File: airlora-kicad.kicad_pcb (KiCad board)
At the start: 4 copper layers, 77 x 77 mm, 128 parts, among them IC1 BALFHB-WL-02D3, J1 12V, J10 I2C, J11 UART2, J2 Conn_Coaxial, J3 Led, J4 SHT, J5 I2C, J6 A_NO2, J7 UART1, J8 A_CO, J9 I2C, Q1 ZVP2106GTA, Q10 S8050, Q2 S8050, Q3 S8050, Q4 S8050, Q5 S8050, Q6 S8050, Q7 S8050, Q8 S8050, Q9 S8050, SW1 SW_Push, SW2 SW_Slide_DPDT, SW3 SW_Push, U1 TPS7A2633DRVR, U2 TPS54202DDC, U3 TPS7A2633DRVR, U4 BGS12WN6E6327, U5 STM32WLE5CCUx, U6 STM32F103C8Tx, X1 NX2016SA-32MHZ, Y1 NX2012SA 32.768KHz, Y2 8Mhz

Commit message: refactored project
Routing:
- net +5V: track 134.0 -> 0.00 mm
- net /AirLora V3/MCU Sub/SDA1: track 80.1 -> 0.00 mm
- net +3.3V_HP: track 70.0 -> 0.00 mm
- net /AirLora V3/MCU Sub/SCL1: track 64.9 -> 0.00 mm
- net /AirLora V3/MCU Sub/RX3: track 41.3 -> 0.00 mm
- net /AirLora V3/MCU Sub/TX3: track 41.2 -> 0.00 mm
- net /AirLora V3/MCU Sub/PA5: track 30.9 -> 0.00 mm
- net /AirLora V3/MCU Sub/PA15: track 21.1 -> 0.00 mm
- net /AirLora V3/MCU Sub/SW_CLK: track 19.4 -> 0.00 mm
- net Net-(U6-NRST): track 16.4 -> 0.00 mm
- net Net-(D1-A): track 15.2 -> 0.00 mm
- net /AirLora V3/MCU Sub/PB4: track 14.9 -> 0.00 mm
- net Net-(J4-Pin_2): track 14.3 -> 0.00 mm
- net +3.3V: track 13.8 -> 0.00 mm
- net Net-(U2-FB): track 13.7 -> 0.00 mm
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- removed copper zone on B.Cu, net GND
- removed copper zone on F.Cu, net GND
- removed copper zone on In1.Cu, net GND
- removed copper zone on In2.Cu, net GND

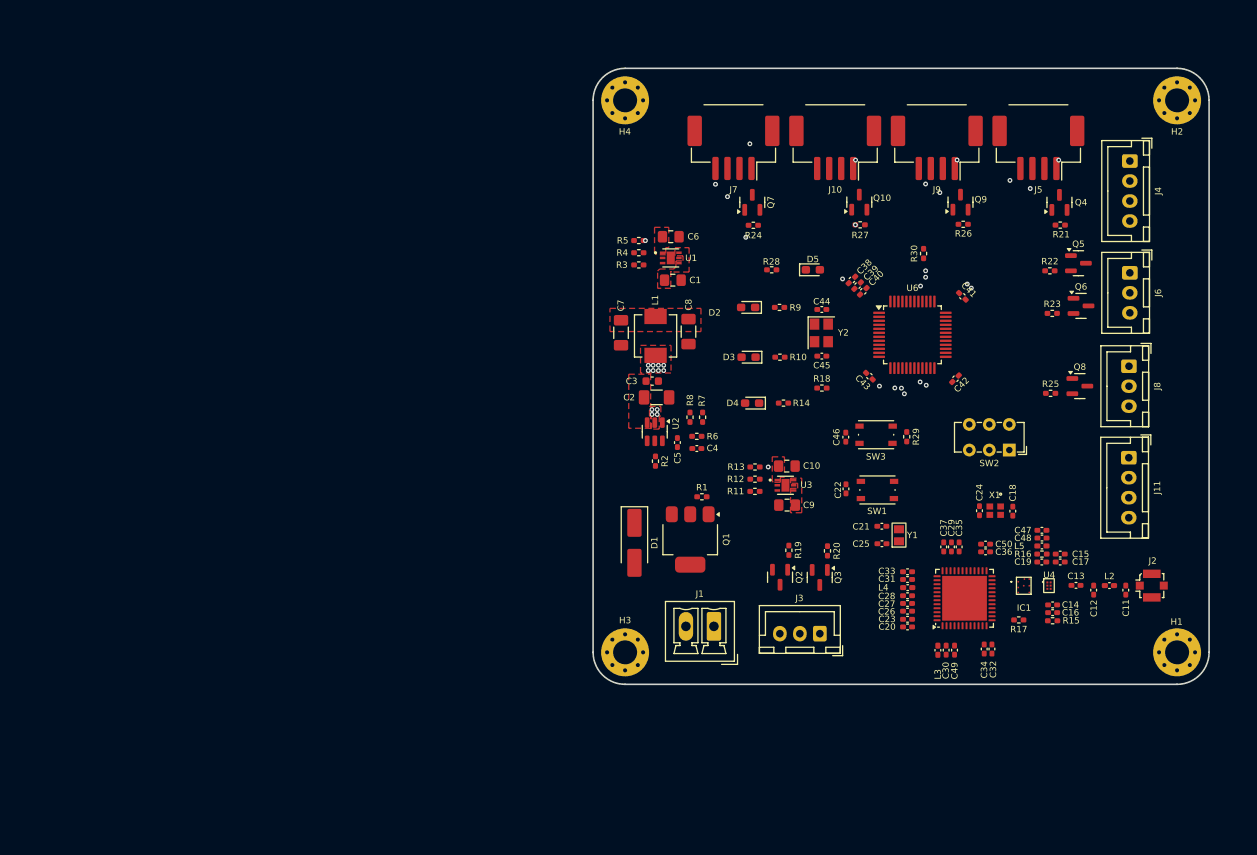
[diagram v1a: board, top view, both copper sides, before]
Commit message: removed polarity protection and fixed component placement
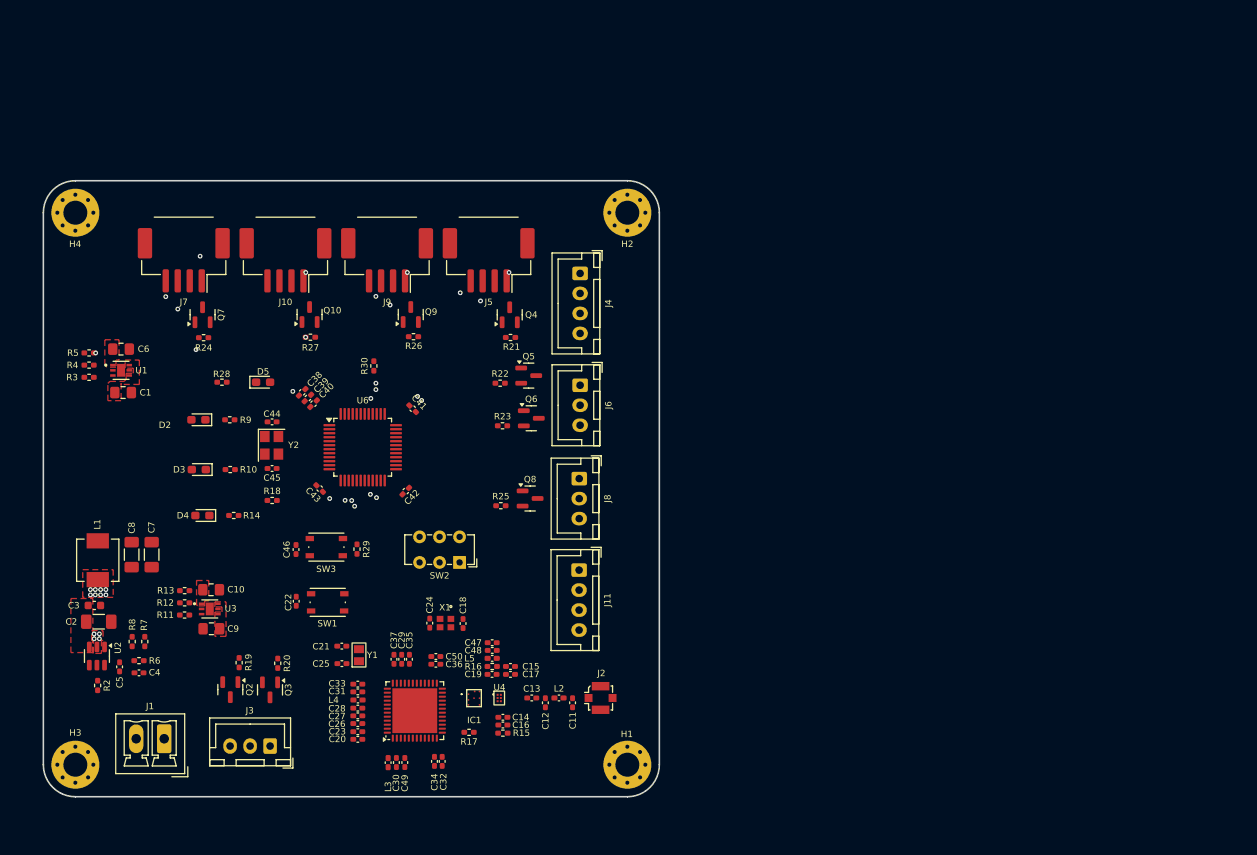
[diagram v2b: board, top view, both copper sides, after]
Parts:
- removed D1: D_Zener, Diode_SMD:D_SMA_Handsoldering
- removed Q1: ZVP2106GTA, Package_TO_SOT_SMD:SOT-223-3_TabPin2
- removed R1: 10K, Resistor_SMD:R_0402_1005Metric_Pad0.72x0.64mm_HandSolder
- C11, C12: value 3.3pF -> NC
- C15, C16: value 10pF -> 100nF
- L2: value 8.7uH -> 0R
- moved C3 75.2 mm to (66.9, 100.9)
- moved L1 75.2 mm to (67.3, 95.2)
- moved R8 75.2 mm to (71.6, 105.4)
- moved C2 75.2 mm to (67.5, 102.9)
- moved C4 75.2 mm to (72.5, 109.3)
- moved C5 75.2 mm to (70.1, 108.6)
- moved R2 75.2 mm to (67.3, 110.9)
- moved R6 75.2 mm to (72.5, 107.8)
- moved R7 75.2 mm to (73.2, 105.4)
- moved U2 75.2 mm to (67.2, 107.2)
- moved C8 75.0 mm to (71.6, 94.5)
- moved C10 73.6 mm to (81.5, 98.9)
- moved C9 73.6 mm to (81.5, 103.8)
- moved U3 73.6 mm to (81.3, 101.3)
- moved R11 72.9 mm to (78.2, 102.1)
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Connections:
- net SW renamed Net-(U2-SW)
- J1 pad 1: Net-(J1-Pin_1) -> +12V
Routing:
- net GND: vias 4 -> 3

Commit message: Update layout PCB
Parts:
- moved C49 1.74 mm to (104.0, 120.5)
- moved C30 1.71 mm to (103.0, 120.5)
- moved L3 1.36 mm to (105.0, 120.5)
- moved C29 0.61 mm to (105.9, 107.6)
- moved C35 0.61 mm to (106.9, 107.6)
- moved C37 0.61 mm to (105.0, 107.6)
- moved R14 0.50 mm to (83.8, 89.6)
- moved D4 0.50 mm to (79.9, 89.6)
- moved C1 0.17 mm to (70.5, 74.1), turned to 180 degrees
- moved D3 0.05 mm to (79.9, 83.9)
- moved R10 0.05 mm to (83.8, 83.9)
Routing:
- net +5V: track 0.00 -> 174.9 mm, vias 4 -> 8
- net +3.3V: track 0.00 -> 128.3 mm, vias 0 -> 5
- net +3.3V_HP: track 0.00 -> 98.8 mm, vias 1 -> 0
- net /AirLora V3/MCU Sub/SCL1: track 0.00 -> 73.8 mm, vias 2 -> 0
- net /AirLora V3/MCU Sub/SDA1: track 0.00 -> 60.0 mm, vias 2 -> 3
- net /AirLora V3/MCU Sub/SCL2: track 0.00 -> 59.1 mm, vias 1 -> 0
- net /AirLora V3/MCU Sub/SDA2: track 0.00 -> 58.4 mm, vias 1 -> 2
- net Net-(U5-PA4): track 0.00 -> 52.8 mm, vias 0 -> 2
- net /AirLora V3/MCU/PA3: track 0.00 -> 52.7 mm, vias 0 -> 2
- net Net-(U5-PA5): track 0.00 -> 47.4 mm
- net /AirLora V3/MCU Sub/TX3: track 0.00 -> 46.5 mm
- net /AirLora V3/MCU Sub/RX3: track 0.00 -> 45.3 mm
- net Net-(U5-PA6): track 0.00 -> 43.4 mm
- net +12V: track 0.00 -> 40.1 mm
- net /AirLora V3/MCU Sub/PB0: track 0.00 -> 36.5 mm, vias 0 -> 1
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- added copper zone on B.Cu, net GND
- added copper zone on F.Cu, net GND
- added copper zone on In1.Cu, net GND
- added copper zone on In2.Cu, net GND

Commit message: Update PCB layout
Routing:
- net +12V: track 40.1 -> 42.0 mm
- net +3.3V: track 128.3 -> 129.1 mm
- net /AirLora V3/MCU Sub/PB0: track 36.5 -> 35.7 mm
- net Net-(J4-Pin_2): track 14.4 -> 15.0 mm
- net /AirLora V3/MCU Sub/PA5: track 34.8 -> 34.2 mm
- net /AirLora V3/MCU Sub/PA7: track 28.2 -> 28.8 mm
- net Net-(J3-Pin_2): track 7.68 -> 7.14 mm
- net GND: vias 36 -> 37

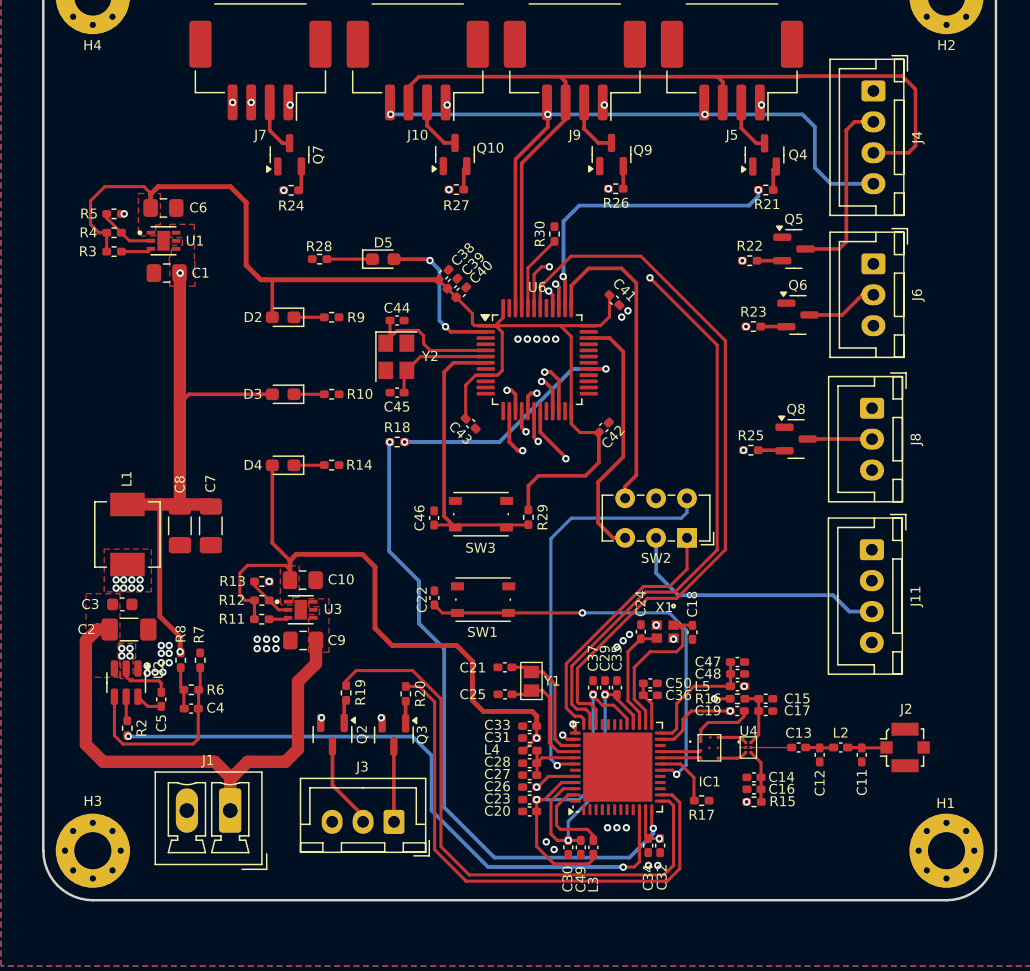
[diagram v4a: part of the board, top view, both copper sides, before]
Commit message: [Fix] Schematic and layout. - Replaced STM32WLE5x symbol for better visualization of the symbols - Added some missing connections - Modified some components' values - Changed the layout for STM32WL
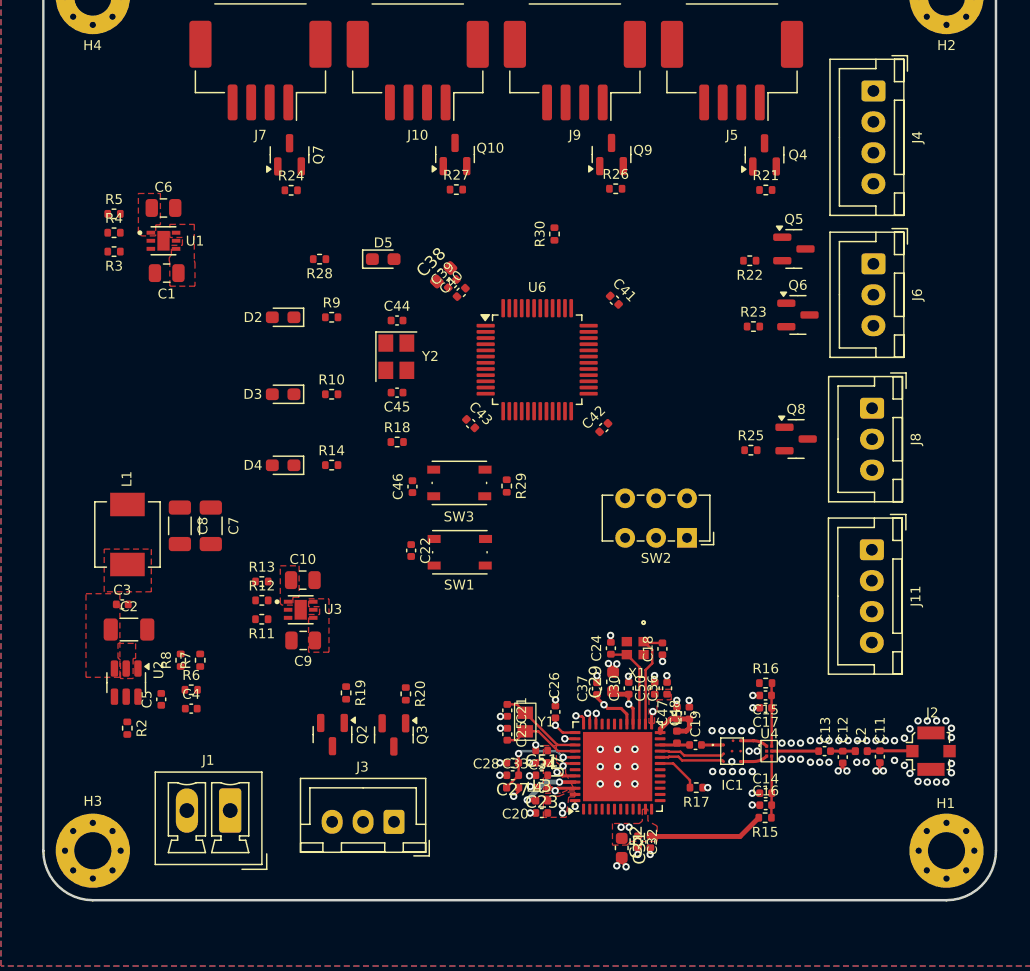
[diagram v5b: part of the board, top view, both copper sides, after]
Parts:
- removed C35, C49: 100pF, Capacitor_SMD:C_0402_1005Metric_Pad0.74x0.62mm_HandSolder
- removed U5: STM32WLE5CCUx, Package_DFN_QFN:QFN-48-1EP_7x7mm_P0.5mm_EP5.6x5.6mm
- added C51: 100nF, Capacitor_SMD:C_0402_1005Metric, F.Cu at (100.8, 114.7)
- added C52: 100nF, Capacitor_SMD:C_0402_1005Metric, F.Cu at (109.6, 120.1)
- added U7: STM32WLE5CCUx, Package_DFN_QFN:QFN-48-1EP_7x7mm_P0.5mm_EP5.6x5.6mm, F.Cu at (106.9, 114.0)
- C1, C10, C6, C9: footprint Capacitor_SMD:C_0805_2012Metric_Pad1.18x1.45mm_HandSolder -> Capacitor_SMD:C_0805_2012Metric
- C11, C12, C14, C15, C16, C17, C18, C19, C20, C21, C22, C24, C25, C26, C27, C28, C30, C32, C33, C34, C36, C37, C39, C4, C40, C41, C42, C43, C44, C45, C46, C5: footprint Capacitor_SMD:C_0402_1005Metric_Pad0.74x0.62mm_HandSolder -> Capacitor_SMD:C_0402_1005Metric
- C13: value 33pF -> 39pF; footprint Capacitor_SMD:C_0402_1005Metric_Pad0.74x0.62mm_HandSolder -> Capacitor_SMD:C_0402_1005Metric
- C2, C7, C8: footprint Capacitor_SMD:C_1206_3216Metric_Pad1.33x1.80mm_HandSolder -> Capacitor_SMD:C_1206_3216Metric
- C23: value 470nF -> 4.7uF; footprint Capacitor_SMD:C_0402_1005Metric_Pad0.74x0.62mm_HandSolder -> Capacitor_SMD:C_0402_1005Metric
- C29, C31: footprint Capacitor_SMD:C_0402_1005Metric_Pad0.74x0.62mm_HandSolder -> Capacitor_SMD:C_0603_1608Metric
- C3: footprint Capacitor_SMD:C_0603_1608Metric -> Capacitor_SMD:C_0402_1005Metric
- C38: value 4.7uf -> 4.7uF; footprint Capacitor_SMD:C_0402_1005Metric_Pad0.74x0.62mm_HandSolder -> Capacitor_SMD:C_0603_1608Metric
- C47: value 0.47uF -> 68pF; footprint Capacitor_SMD:C_0402_1005Metric_Pad0.74x0.62mm_HandSolder -> Capacitor_SMD:C_0402_1005Metric
- C48: value 470nF -> 47nF; footprint Capacitor_SMD:C_0402_1005Metric_Pad0.74x0.62mm_HandSolder -> Capacitor_SMD:C_0402_1005Metric
- C50: value 100pF -> 100nF; footprint Capacitor_SMD:C_0402_1005Metric_Pad0.74x0.62mm_HandSolder -> Capacitor_SMD:C_0402_1005Metric
- L2, L3, L4: footprint Inductor_SMD:L_0402_1005Metric_Pad0.77x0.64mm_HandSolder -> Inductor_SMD:L_0402_1005Metric
- L5: value NC -> 47nH; footprint Inductor_SMD:L_0402_1005Metric_Pad0.77x0.64mm_HandSolder -> Inductor_SMD:L_0402_1005Metric
- R10, R11, R12, R13, R14, R15, R16, R17, R18, R19, R2, R20, R21, R22, R23, R24, R25, R26, R27, R28, R29, R3, R30, R4, R5, R6, R7, R8, R9: footprint Resistor_SMD:R_0402_1005Metric_Pad0.72x0.64mm_HandSolder -> Resistor_SMD:R_0402_1005Metric
- X1: value NX2016SA-32MHZ -> 32MHZ
- Y1: value NX2012SA 32.768KHz -> 32.768kHz
- moved C30 13.8 mm to (107.8, 107.7), turned to 90 degrees
- moved C31 11.6 mm to (107.3, 120.6), turned to -90 degrees
- moved C34 11.5 mm to (100.8, 112.7), turned to 180 degrees
- moved C26 6.42 mm to (101.9, 109.6), turned to 90 degrees
- moved C47 6.40 mm to (111.7, 109.7), turned to 90 degrees
- moved L5 6.39 mm to (111.7, 111.6), turned to -90 degrees
- moved L3 5.63 mm to (100.8, 116.7), turned to 0 degrees
- moved C48 5.02 mm to (112.7, 109.7), turned to 90 degrees
- moved C19 4.35 mm to (113.2, 112.2)
- moved C22 4.27 mm to (90.3, 96.5)
- moved SW1 4.27 mm to (94.2, 96.7)
- moved C21 3.48 mm to (98.0, 109.4), turned to -90 degrees
- moved Y1 3.33 mm to (99.5, 110.4)
- moved L4 3.30 mm to (98.5, 115.7), turned to 180 degrees
- moved C25 3.23 mm to (98.0, 111.4), turned to -90 degrees
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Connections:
- net Net-(U5-NRST) renamed /AirLora V3/MCU/NRST
- net Net-(U5-VDDA) renamed /AirLora V3/MCU/VDDA
- net Net-(U5-VR_PA) renamed /AirLora V3/MCU/VR_PA
- net RFO_IN renamed /AirLora V3/MCU/RFO_LP
- C20 pad 1: VDDRF1V55 -> /AirLora V3/MCU/VDDRF1V55
- C21 pad 1: GND -> Net-(U7-PC14_OSC32_IN)
- C21 pad 2: Net-(U5-PC14) -> GND
- C23 pad 1: VDDRF1V55 -> +3.3V
- C29 pad 1: VDDRF -> +3.3V
- C30 pad 1: VDDRF -> +3.3V
- C36 pad 1: VDDPA -> /AirLora V3/MCU/VDDRF1V55
- C37 pad 1: VDDRF1V55 -> /AirLora V3/MCU/VDDRF1V55
- C50 pad 1: VDDPA -> /AirLora V3/MCU/VDDRF1V55
- IC1 pad A2: Net-(IC1-RFI_N_OUT) -> /AirLora V3/MCU/RFI_N
- IC1 pad A3: Net-(IC1-RFI_P_OUT) -> /AirLora V3/MCU/RFI_P
- L3 pad 1: VDDRF1V55 -> Net-(U7-VFBSMPS)
- L3 pad 2: Net-(U5-VLXSMPS) -> /AirLora V3/MCU/VDDRF1V55
- R15 pad 1: +3.3V -> Net-(U4-VDD)
- R15 pad 2: Net-(U4-VDD) -> +3.3V
- R16 pad 1: Net-(U5-PC13) -> /AirLora V3/MCU/FE_CTRL1
- R19 pad 1: Net-(U5-PA5) -> /AirLora V3/MCU/PA5
- R20 pad 1: Net-(U5-PA6) -> /AirLora V3/MCU/PA6
- Y1 pad 2: Net-(U5-PC14) -> Net-(U7-PC14_OSC32_IN)
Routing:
- net +5V: track 174.9 -> 0.00 mm, vias 8 -> 0
- net +3.3V: track 129.1 -> 20.7 mm, vias 5 -> 7
- net +3.3V_HP: track 98.8 -> 0.00 mm
- net /AirLora V3/MCU Sub/SCL1: track 73.8 -> 0.00 mm
- net /AirLora V3/MCU Sub/SDA1: track 60.0 -> 0.00 mm, vias 3 -> 0
- net /AirLora V3/MCU Sub/SCL2: track 59.1 -> 0.88 mm, vias 0 -> 1
- net /AirLora V3/MCU Sub/SDA2: track 58.4 -> 0.95 mm, vias 2 -> 1
- net Net-(U7-PA4): track 52.8 -> 0.00 mm, vias 2 -> 0
- net /AirLora V3/MCU/PA3: track 52.7 -> 0.00 mm, vias 2 -> 0
- net Net-(U5-PA5): track 47.4 -> 0.00 mm
- net /AirLora V3/MCU Sub/TX3: track 46.5 -> 0.00 mm, vias 2 -> 0
- net /AirLora V3/MCU Sub/RX3: track 45.8 -> 0.00 mm, vias 2 -> 0
- net Net-(U5-PA6): track 43.2 -> 0.00 mm
- net +12V: track 42.0 -> 0.00 mm
- net /AirLora V3/MCU Sub/PB0: track 35.7 -> 0.00 mm, vias 1 -> 0
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- added copper zone on In2.Cu, net +3.3V
- added copper zone on F.Cu, net /AirLora V3/MCU/VDDRF1V55
- added copper zone on In2.Cu, net /AirLora V3/MCU/VDDRF1V55

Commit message: Update PCB layout
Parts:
- SW1: footprint Button_Switch_SMD:SW_Push_1P1T_NO_Vertical_Wuerth_434133025816 -> Button_Switch_THT:SW_Tactile_SPST_Angled_PTS645Vx39-2LFS
- SW3: footprint Button_Switch_SMD:SW_Push_1P1T_NO_Vertical_Wuerth_434133025816 -> Button_Switch_SMD:SW_Tactile_SPST_NO_Straight_CK_PTS636Sx25SMTRLFS
- moved SW1 41.6 mm to (127.5, 121.5), turned to 180 degrees
- moved C22 38.1 mm to (118.9, 121.6), turned to 180 degrees
- moved R18 19.2 mm to (108.0, 84.2)
- moved R29 7.11 mm to (90.9, 92.3)
- moved SW3 3.14 mm to (96.7, 92.9), turned to 180 degrees
- moved SW2 2.77 mm to (115.3, 95.9)
- moved R2 2.66 mm to (64.8, 110.2)
- moved R23 2.40 mm to (118.3, 80.8)
- moved Q6 2.10 mm to (121.4, 79.6)
- moved R28 1.79 mm to (84.6, 73.0)
- moved C46 1.12 mm to (89.8, 92.3)
- moved C41 1.02 mm to (105.7, 76.3)
- moved R30 0.88 mm to (101.0, 71.3), turned to 0 degrees
- moved R24 0.78 mm to (81.2, 67.0)
- moved R27 0.77 mm to (94.6, 67.0)
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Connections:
- C18 pad 2: Net-(U7-OSC_OUT) -> Net-(U7-OSC_IN)
- C24 pad 1: Net-(U7-OSC_IN) -> Net-(U7-OSC_OUT)
- J7 pad 3: /AirLora V3/MCU Sub/RX3 -> /AirLora V3/MCU Sub/TX3
- J7 pad 4: /AirLora V3/MCU Sub/TX3 -> /AirLora V3/MCU Sub/RX3
- X1 pad 1: Net-(U7-OSC_OUT) -> Net-(U7-OSC_IN)
- X1 pad 3: Net-(U7-OSC_IN) -> Net-(U7-OSC_OUT)
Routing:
- net +5V: track 0.00 -> 191.1 mm, vias 0 -> 3
- net +3.3V: track 20.7 -> 104.0 mm, vias 7 -> 9
- net +3.3V_HP: track 0.00 -> 73.2 mm, vias 0 -> 12
- net /AirLora V3/MCU Sub/SDA1: track 0.00 -> 61.7 mm, vias 0 -> 3
- net /AirLora V3/MCU Sub/SCL1: track 0.00 -> 61.0 mm, vias 0 -> 3
- net /AirLora V3/MCU Sub/RX3: track 0.00 -> 54.6 mm
- net /AirLora V3/MCU Sub/TX3: track 0.00 -> 51.1 mm
- net /AirLora V3/MCU/PA3: track 0.00 -> 49.0 mm, vias 0 -> 2
- net +12V: track 0.00 -> 44.2 mm
- net Net-(U7-PA4): track 0.00 -> 44.0 mm, vias 0 -> 3
- net /AirLora V3/MCU Sub/SDA2: track 0.95 -> 39.1 mm, vias 1 -> 2
- net /AirLora V3/MCU Sub/SCL2: track 0.88 -> 38.9 mm, vias 1 -> 2
- net /AirLora V3/MCU/PA5: track 0.00 -> 36.4 mm, vias 0 -> 2
- net /AirLora V3/MCU/T_SWCLK: track 1.06 -> 34.3 mm
- net /AirLora V3/MCU/PA6: track 0.00 -> 33.0 mm, vias 0 -> 2
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- added copper zone on In2.Cu, net +3.3V_HP
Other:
- outline, holes or cut-outs redrawn
